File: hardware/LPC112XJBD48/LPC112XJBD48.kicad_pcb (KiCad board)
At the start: 2 copper layers, 2 parts

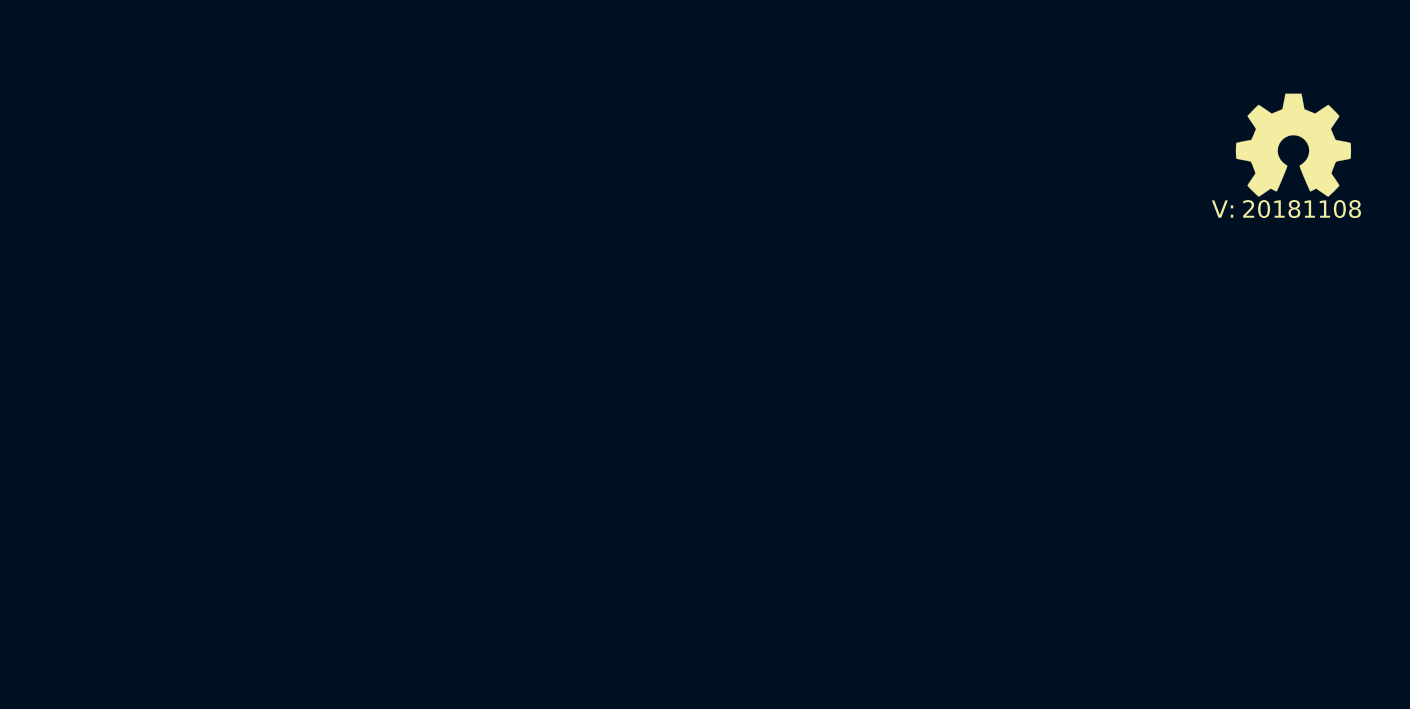
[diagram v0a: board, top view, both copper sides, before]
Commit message: copied LPC824 breakout to LPC1125
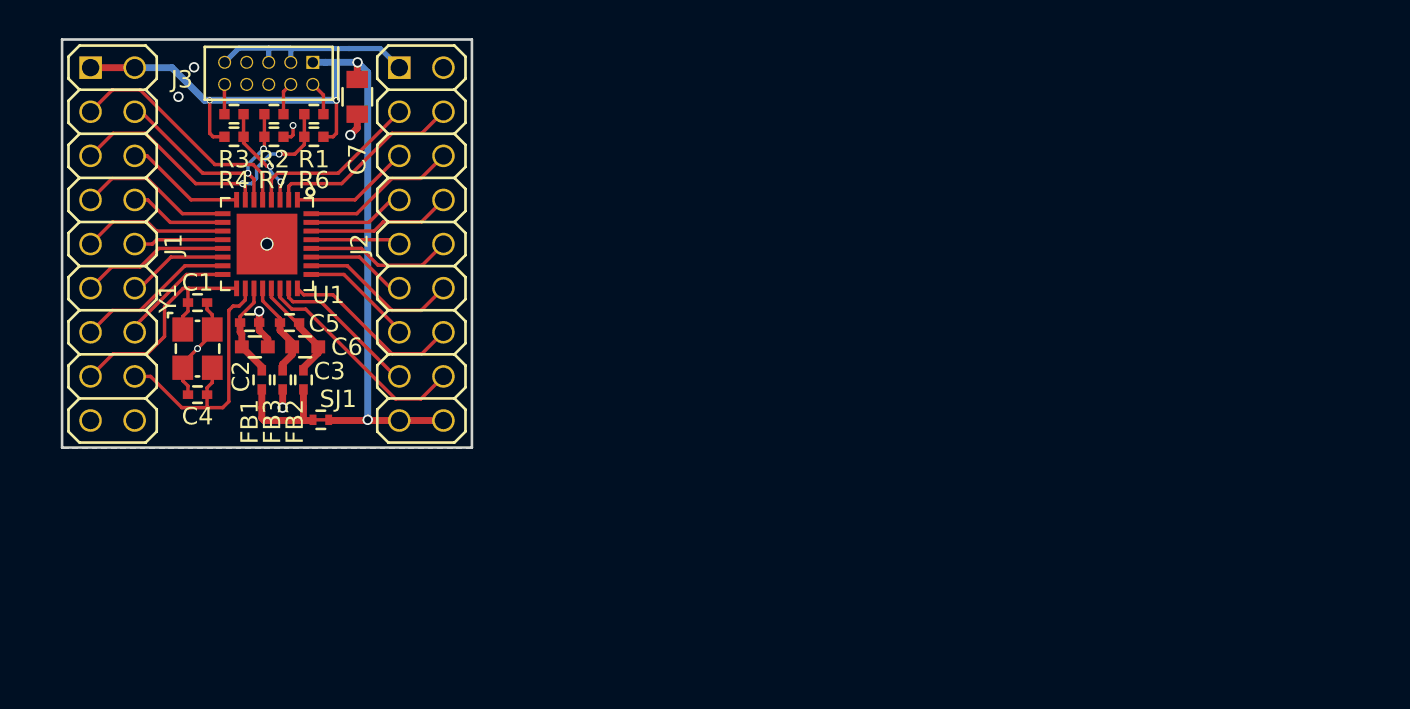
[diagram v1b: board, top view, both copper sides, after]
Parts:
- added C1: 18p, SquantorRcl:C_0402, F.Cu at (84.9, 110.0)
- added C2: 1u, SquantorRcl:C_0603, F.Cu at (88.2, 112.6)
- added C3: 1u, SquantorRcl:C_0603, F.Cu at (91.1, 112.6)
- added C4: 18p, SquantorRcl:C_0402, F.Cu at (84.9, 115.3)
- added C5: 100n, SquantorRcl:C_0402, F.Cu at (87.9, 111.2)
- added C6: 100n, SquantorRcl:C_0402, F.Cu at (90.2, 111.2)
- added C7: 10u, SquantorRcl:C_0805, F.Cu at (94.1, 98.2)
- added FB1: FB, SquantorRcl:C_0402, F.Cu at (88.6, 114.5)
- added FB2: FB, SquantorRcl:C_0402, F.Cu at (91.0, 114.5)
- added FB3: FB, SquantorRcl:C_0402, F.Cu at (89.8, 114.5)
- added J1: Conn_02x09_Odd_Even, SquantorConnectors:Header-0254-2X09-H010, F.Cu at (80.0, 106.7)
- added J2: Conn_02x09_Odd_Even, SquantorConnectors:Header-0254-2X09-H010, F.Cu at (97.8, 106.7)
- added J3: JTAG_2X05, SquantorConnectors:Header-0127-2X05-H006, F.Cu at (89.0, 96.8)
- added R1: 100, SquantorRcl:R_0402_hand, F.Cu at (91.6, 99.2)
- added R2: 100, SquantorRcl:R_0402_hand, F.Cu at (89.3, 99.2)
- added R3: 100, SquantorRcl:R_0402_hand, F.Cu at (87.0, 99.2)
- added R4: 100K, SquantorRcl:R_0402_hand, F.Cu at (87.0, 100.5)
- added R6: 100k, SquantorRcl:R_0402_hand, F.Cu at (91.6, 100.5)
- added R7: 100k, SquantorRcl:R_0402_hand, F.Cu at (89.3, 100.5)
- added SJ1: SolderJumper_2way_1conn, SquantorSpecial:solder_jumper_2way_conn, F.Cu at (92.0, 116.8)
- added U1: LPC824M201JHI33, SquantorIC:SOT617-3, F.Cu at (88.9, 106.7)
- added Y1: 12MHz, SquantorCrystal:Crystal_3225_4, F.Cu at (84.9, 112.7)
- N1: moved to B.Cu
- N2: value 20181108 -> 20181124; moved to B.Cu
- moved N1 59.6 mm to (88.7, 106.7), turned to 270 degrees
- moved N2 56.4 mm to (92.6, 108.0), turned to 270 degrees
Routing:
- net VDD: track 0.00 -> 53.8 mm, vias 0 -> 4
- net VSS: track 0.00 -> 24.8 mm, vias 0 -> 8
- net /PIO0_2: track 0.00 -> 18.1 mm, vias 0 -> 2
- net /PIO0_8: track 0.00 -> 16.1 mm
- net /PIO0_9: track 0.00 -> 14.3 mm
- net /PIO0_28: track 0.00 -> 13.9 mm
- net /PIO0_3: track 0.00 -> 13.5 mm, vias 0 -> 2
- net /PIO0_7: track 0.00 -> 12.9 mm
- net /PIO0_12: track 0.00 -> 11.5 mm
- net /PIO0_0: track 0.00 -> 10.5 mm
- net /PIO0_4: track 0.00 -> 10.2 mm
- net /PIO0_23: track 0.00 -> 9.20 mm
- net /PIO0_15: track 0.00 -> 9.20 mm
- net /PIO0_17: track 0.00 -> 8.99 mm
- net /PIO0_10: track 0.00 -> 8.96 mm
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- added copper zone on B.Cu, net VSS
- added copper zone on F.Cu, net VSS
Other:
- board outline added: 23.6 x 23.5 mm
- net class Default: clearance 0.1524 -> 0.127; trace_width 0.1524 -> 0.127; via_dia 0.381 -> 0.3556
- rule solder_mask_min_width: 0.15 -> 0.2
- rule trace_clearance: 0.1524 -> 0.127
- rule trace_min: 0.1524 -> 0.127
- rule via_min_size: 0.381 -> 0.3556

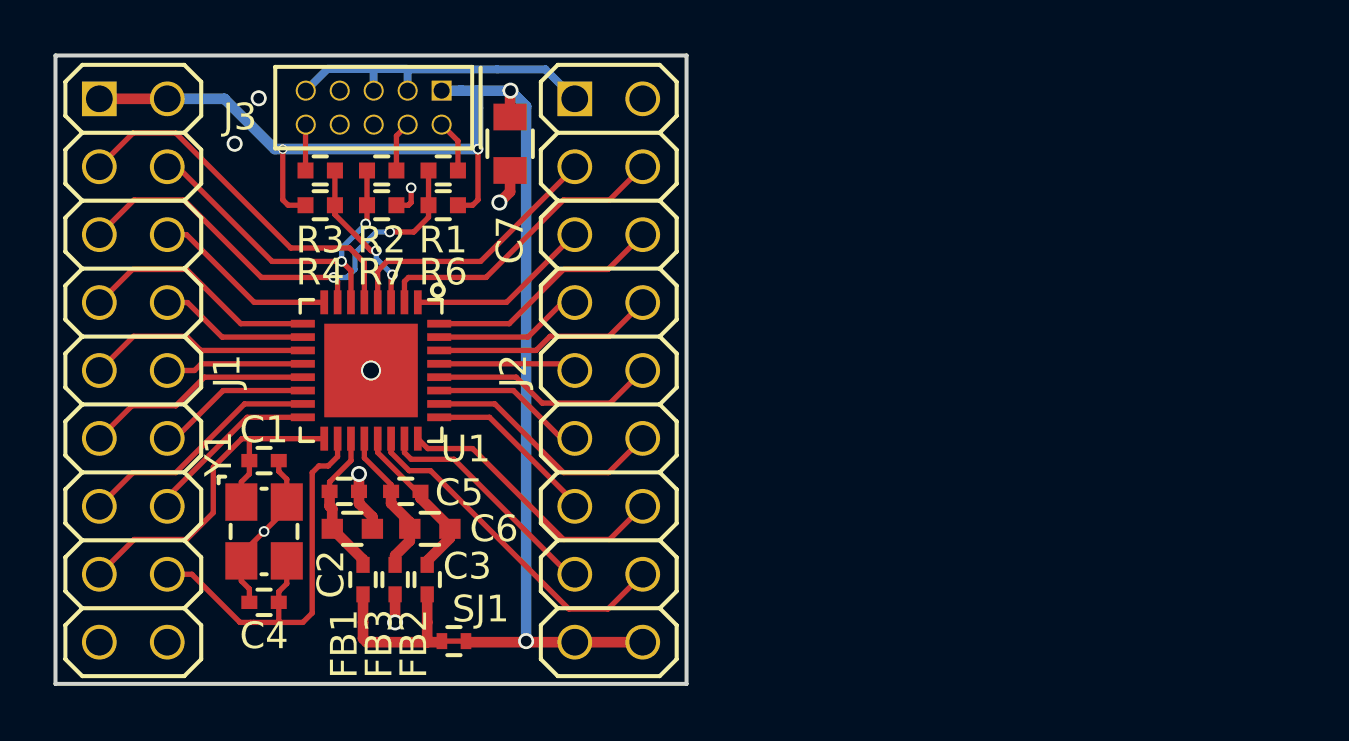
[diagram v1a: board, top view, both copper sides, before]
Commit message: schematic entry in progress, added LPC1125
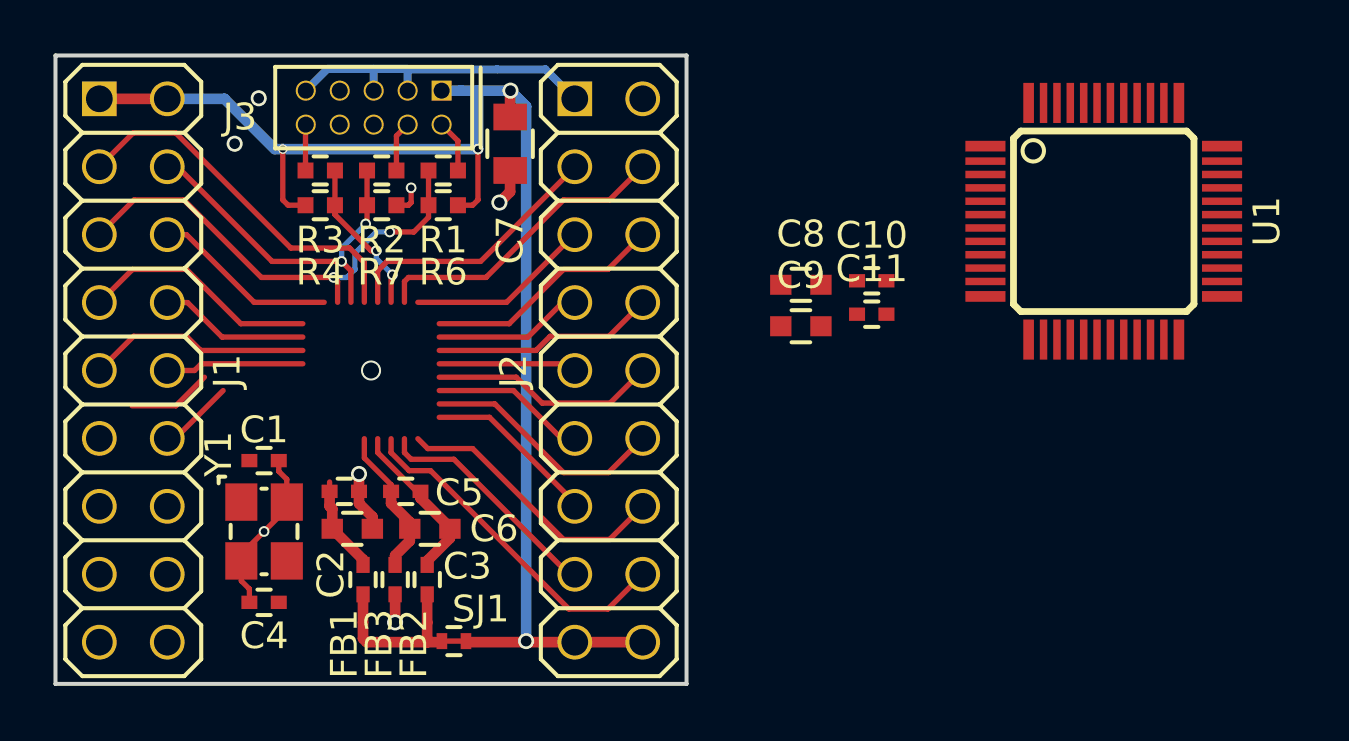
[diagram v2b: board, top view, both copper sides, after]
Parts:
- added C10: 100n, SquantorRcl:C_0402, F.Cu at (107.6, 103.3)
- added C11: 100n, SquantorRcl:C_0402, F.Cu at (107.6, 104.6)
- added C8: 1u, SquantorRcl:C_0603, F.Cu at (105.0, 103.5)
- added C9: 1u, SquantorRcl:C_0603, F.Cu at (105.0, 105.0)
- FB1, FB2, FB3: value FB -> 600
- N2: value 20181124 -> 20190310
- U1: value LPC824M201JHI33 -> LPC1125JBD48_303; footprint SquantorIC:SOT617-3 -> SquantorIC:SOT313-2-NXP
- moved U1 28.0 mm to (116.3, 101.1)
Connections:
- C1 pad 1: /PIO0_9 -> /XTALOUT
- C2 pad 1: Net-(C2-Pad1) -> Net-(C10-Pad1)
- C3 pad 1: Net-(C3-Pad1) -> Net-(C11-Pad1)
- C3 pad 2: Net-(C3-Pad2) -> Net-(C11-Pad2)
- C4 pad 1: /PIO0_8 -> /XTALIN
- C5 pad 1: Net-(C2-Pad1) -> Net-(C10-Pad1)
- C6 pad 1: Net-(C3-Pad1) -> Net-(C11-Pad1)
- C6 pad 2: Net-(C3-Pad2) -> Net-(C11-Pad2)
- FB1 pad 1: Net-(C2-Pad1) -> Net-(C10-Pad1)
- FB2 pad 1: Net-(C3-Pad1) -> Net-(C11-Pad1)
- FB3 pad 1: Net-(C3-Pad2) -> Net-(C11-Pad2)
- J1 pad 10: /PIO0_26 -> (no net)
- J1 pad 11: /PIO0_25 -> (no net)
- J1 pad 12: /PIO0_24 -> (no net)
- J1 pad 13: /PIO0_15 -> (no net)
- J1 pad 14: /PIO0_1 -> (no net)
- J1 pad 15: /PIO0_9 -> (no net)
- J1 pad 16: /PIO0_8 -> (no net)
- J1 pad 3: /PIO0_28 -> (no net)
- J1 pad 4: /PIO0_3 -> (no net)
- J1 pad 5: /PIO0_2 -> (no net)
- J1 pad 6: /PIO0_11 -> (no net)
- J1 pad 8: /PIO0_16 -> (no net)
- J1 pad 9: /PIO0_27 -> (no net)
- J2 pad 10: /PIO0_21 -> (no net)
- J2 pad 11: /PIO0_22 -> (no net)
- J2 pad 12: /PIO0_23 -> (no net)
- J2 pad 13: /PIO0_14 -> (no net)
- J2 pad 14: /PIO0_0 -> (no net)
- J2 pad 15: /PIO0_6 -> (no net)
- J2 pad 16: /PIO0_7 -> (no net)
- J2 pad 3: /PIO0_4 -> (no net)
- J2 pad 4: /PIO0_12 -> (no net)
- J2 pad 5: /PIO0_13 -> (no net)
- J2 pad 6: /PIO0_17 -> (no net)
- J2 pad 7: /PIO0_18 -> (no net)
- J2 pad 8: /PIO0_19 -> (no net)
- J2 pad 9: /PIO0_20 -> (no net)
- R1 pad 2: /PIO0_2 -> /PIO1_3
- R2 pad 2: /PIO0_3 -> /PIO0_10
- R6 pad 2: /PIO0_2 -> /PIO1_3
- R7 pad 2: /PIO0_3 -> /PIO0_10
- SJ1 pad 1: VDD -> Net-(FB1-Pad2)
- SJ1 pad 2: Net-(FB1-Pad2) -> VDD
- U1 pad 1: /PIO0_13 -> (no net)
- U1 pad 10: /PIO0_16 -> (no net)
- U1 pad 11: /PIO0_27 -> (no net)
- U1 pad 12: /PIO0_26 -> (no net)
- U1 pad 13: /PIO0_25 -> (no net)
- U1 pad 14: /PIO0_24 -> (no net)
- U1 pad 15: /PIO0_15 -> (no net)
- U1 pad 16: /PIO0_1 -> (no net)
- U1 pad 17: /PIO0_9 -> (no net)
- U1 pad 18: /PIO0_8 -> (no net)
- U1 pad 19: Net-(C2-Pad1) -> (no net)
- U1 pad 2: /PIO0_12 -> (no net)
- U1 pad 20: Net-(C3-Pad2) -> (no net)
- U1 pad 21: Net-(C3-Pad1) -> (no net)
- U1 pad 22: /PIO0_7 -> (no net)
- U1 pad 23: /PIO0_6 -> (no net)
- U1 pad 24: /PIO0_0 -> (no net)
- U1 pad 25: /PIO0_14 -> (no net)
- U1 pad 26: /PIO0_23 -> (no net)
- U1 pad 27: /PIO0_22 -> (no net)
- U1 pad 28: /PIO0_21 -> /PIO0_10
- U1 pad 29: /PIO0_20 -> (no net)
- U1 pad 30: /PIO0_19 -> (no net)
- U1 pad 31: /PIO0_18 -> (no net)
- U1 pad 32: /PIO0_17 -> (no net)
- U1 pad 33: VSS -> Net-(C11-Pad1)
- U1 pad 4: /PIO0_4 -> (no net)
- U1 pad 5: /PIO0_28 -> VSS
- U1 pad 6: /PIO0_3 -> /XTALIN
- U1 pad 7: /PIO0_2 -> /XTALOUT
- U1 pad 8: /PIO0_11 -> Net-(C10-Pad1)
- U1 pad 9: /PIO0_10 -> (no net)
- Y1 pad 1: /PIO0_9 -> /XTALOUT
- Y1 pad 3: /PIO0_8 -> /XTALIN
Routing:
- net (no net): track 0.00 -> 165.2 mm
- net /PIO0_8: track 16.1 -> 0.00 mm
- net /PIO0_9: track 14.3 -> 0.00 mm
- net /PIO0_28: track 13.9 -> 0.00 mm
- net /PIO0_7: track 12.9 -> 0.00 mm
- net /PIO0_12: track 11.5 -> 0.00 mm
- net /PIO0_0: track 10.5 -> 0.00 mm
- net /PIO0_4: track 10.2 -> 0.00 mm
- net /PIO0_23: track 9.20 -> 0.00 mm
- net /PIO0_15: track 9.20 -> 0.00 mm
- net /PIO0_17: track 8.99 -> 0.00 mm
- net /PIO0_6: track 8.77 -> 0.00 mm
- net /PIO0_25: track 8.56 -> 0.00 mm
- net /PIO0_21: track 8.52 -> 0.00 mm
- net /PIO0_27: track 8.36 -> 0.00 mm
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
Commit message: further placement of components
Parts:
- removed C8, C9: 1u, SquantorRcl:C_0603
- C2, C3: footprint SquantorRcl:C_0603 -> SquantorRcl:C_0402
- C7: footprint SquantorRcl:C_0805 -> SquantorRcl:C_0603
- J1, J2: value Conn_02x09_Odd_Even -> Conn_02x14_Odd_Even; footprint SquantorConnectors:Header-0254-2X09-H010 -> Connector_PinHeader_2.54mm:PinHeader_2x14_P2.54mm_Vertical; moved to B.Cu
- N2: value 20190310 -> 20190512
- moved U1 31.0 mm to (88.9, 115.6), turned to 225 degrees
- moved C11 19.5 mm to (94.3, 118.8), turned to 45 degrees
- moved C10 14.6 mm to (94.6, 109.9), turned to 315 degrees
- moved SJ1 13.6 mm to (88.8, 103.6)
- moved J2 10.5 mm to (100.3, 96.5), turned to 180 degrees
- moved J1 10.2 mm to (80.0, 96.5), turned to 180 degrees
- moved FB3 9.36 mm to (87.6, 105.4)
- moved FB1 9.05 mm to (88.8, 105.5)
- moved FB2 9.04 mm to (90.1, 105.5)
- moved Y1 6.68 mm to (83.9, 106.1)
- moved C1 6.68 mm to (83.9, 103.5)
- moved C4 6.68 mm to (83.9, 108.8)
- moved C3 5.51 mm to (89.6, 107.3)
- moved C2 5.38 mm to (87.3, 107.3)
- moved C5 4.40 mm to (83.5, 111.1), turned to 45 degrees
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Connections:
- J1 pad 10: (no net) -> /PIO2_7
- J1 pad 11: (no net) -> /PIO2_8
- J1 pad 12: (no net) -> VSS
- J1 pad 13: (no net) -> /PIO2_1
- J1 pad 14: (no net) -> /PIO0_3
- J1 pad 15: (no net) -> /PIO0_4
- J1 pad 16: (no net) -> /PIO0_5
- J1 pad 18: VSS -> /PIO1_9
- J1 pad 3: (no net) -> /PIO2_6
- J1 pad 4: (no net) -> /PIO2_0
- J1 pad 5: (no net) -> /RESET
- J1 pad 6: (no net) -> /PIO0_1
- J1 pad 7: /PIO0_10 -> VSS
- J1 pad 8: (no net) -> /PIO1_8
- J1 pad 9: (no net) -> /PIO0_2
- J2 pad 10: (no net) -> /PIO1_3
- J2 pad 11: (no net) -> /PIO2_3
- J2 pad 12: (no net) -> VSS
- J2 pad 13: (no net) -> /PIO3_0
- J2 pad 14: (no net) -> /PIO1_2
- J2 pad 15: (no net) -> /PIO1_1
- J2 pad 16: (no net) -> /PIO1_0
- J2 pad 17: VDD -> VSS
- J2 pad 18: VDD -> /PIO0_11
- J2 pad 3: (no net) -> /PIO3_3
- J2 pad 4: (no net) -> /PIO1_7
- J2 pad 5: (no net) -> /PIO1_6
- J2 pad 6: (no net) -> /PIO1_5
- J2 pad 7: (no net) -> VSS
- J2 pad 8: (no net) -> /PIO1_11
- J2 pad 9: (no net) -> /PIO1_4
- U1 pad 1: (no net) -> /PIO2_6
- U1 pad 10: (no net) -> /PIO0_2
- U1 pad 11: (no net) -> /PIO2_7
- U1 pad 12: (no net) -> /PIO2_8
- U1 pad 13: (no net) -> /PIO2_1
- U1 pad 14: (no net) -> /PIO0_3
- U1 pad 15: (no net) -> /PIO0_4
- U1 pad 16: (no net) -> /PIO0_5
- U1 pad 17: (no net) -> /PIO1_9
- U1 pad 18: (no net) -> /PIO3_4
- U1 pad 19: (no net) -> /PIO2_4
- U1 pad 2: (no net) -> /PIO2_0
- U1 pad 20: (no net) -> /PIO2_5
- U1 pad 21: (no net) -> /PIO3_5
- U1 pad 22: (no net) -> /PIO0_6
- U1 pad 23: (no net) -> /PIO0_7
- U1 pad 24: (no net) -> /PIO2_9
- U1 pad 25: (no net) -> /PIO2_2
- U1 pad 26: (no net) -> /PIO0_8
- U1 pad 27: (no net) -> /PIO0_9
- U1 pad 29: (no net) -> /PIO1_10
- U1 pad 30: (no net) -> /PIO0_11
- U1 pad 31: (no net) -> /PIO1_0
- U1 pad 32: (no net) -> /PIO1_1
- U1 pad 35: (no net) -> /PIO1_2
- U1 pad 36: (no net) -> /PIO3_0
- U1 pad 37: (no net) -> /PIO2_3
- U1 pad 39: (no net) -> /PIO1_4
- U1 pad 4: (no net) -> /PIO0_1
- U1 pad 42: (no net) -> /PIO1_11
- U1 pad 45: (no net) -> /PIO1_5
- U1 pad 46: (no net) -> /PIO1_6
- U1 pad 47: (no net) -> /PIO1_7
- U1 pad 48: (no net) -> /PIO3_3
- U1 pad 9: (no net) -> /PIO1_8
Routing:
- net (no net): track 165.2 -> 0.00 mm
- net VDD: track 53.8 -> 0.00 mm, vias 4 -> 0
- net VSS: track 24.8 -> 1.14 mm, vias 7 -> 1
- net /PIO0_2: track 18.1 -> 0.00 mm, vias 2 -> 0
- net /PIO0_3: track 13.5 -> 0.00 mm, vias 2 -> 0
- net /PIO0_10: track 8.96 -> 0.00 mm
- net Net-(FB1-Pad2): track 6.46 -> 0.00 mm
- net Net-(C11-Pad1): track 6.28 -> 0.00 mm, vias 1 -> 0
- net /RESET: track 6.06 -> 0.00 mm, vias 2 -> 0
- net Net-(C11-Pad2): track 5.65 -> 0.00 mm
- net Net-(C10-Pad1): track 3.62 -> 0.00 mm
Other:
- board size 23.6 x 23.5 mm -> 26.7 x 36.7 mm
